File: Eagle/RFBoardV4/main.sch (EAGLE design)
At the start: 32 parts, among them Q1 8/16/20MHz, U1 ATMEGA328

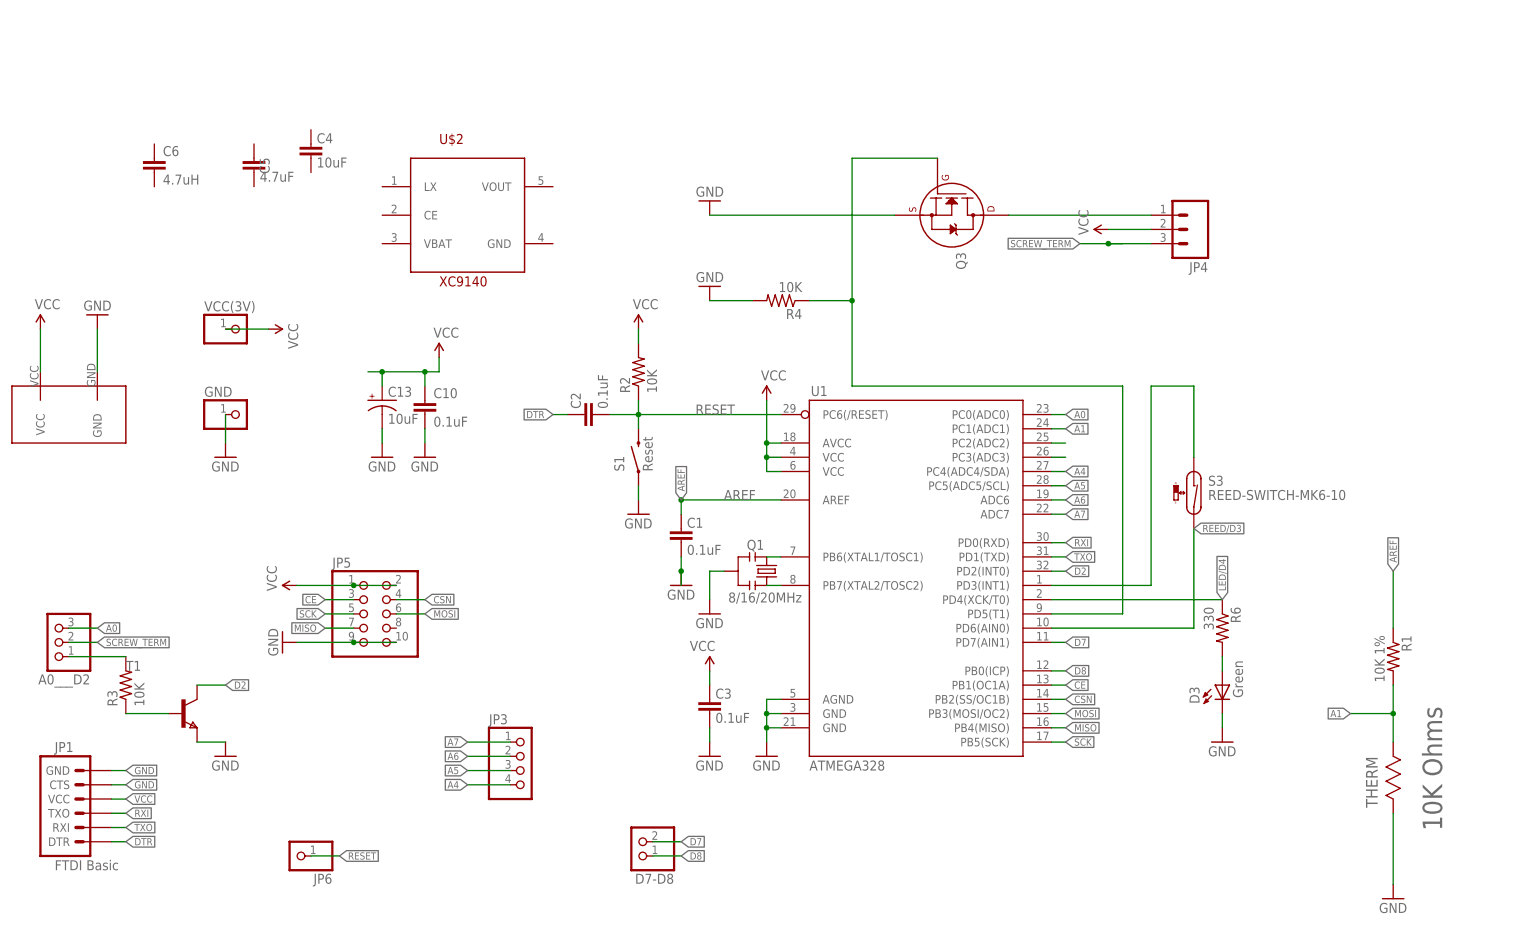
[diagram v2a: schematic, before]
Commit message: Added 3.3v boost circuit to output
- removed transistor that turns aux power on/off
- used boost IC instead
- The aux power now has 3.3v and is useful for PIR solutions
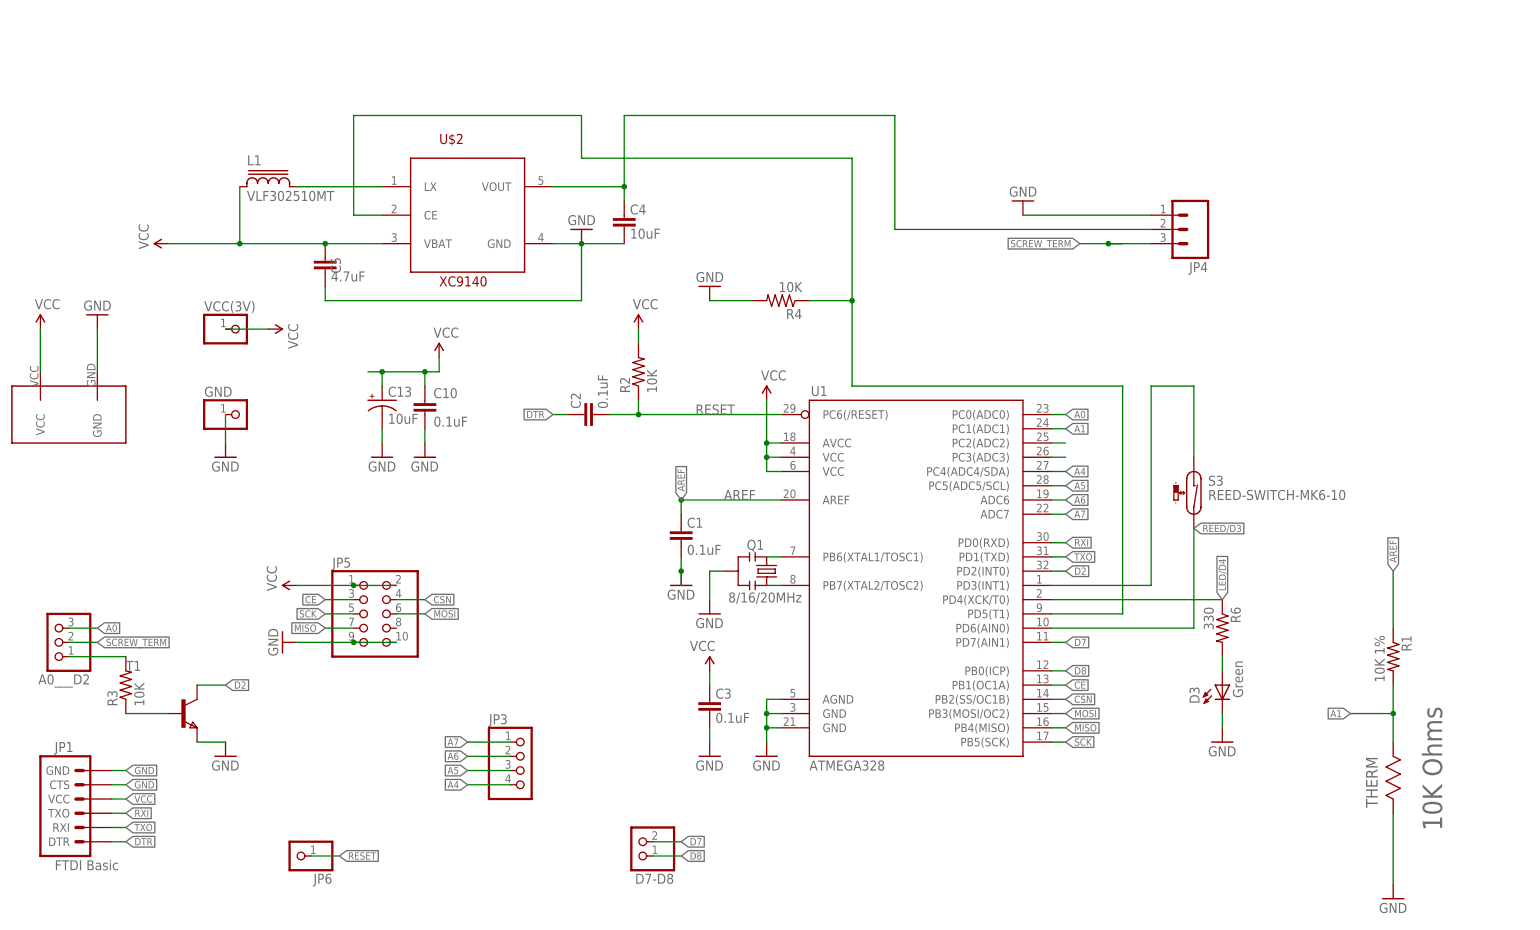
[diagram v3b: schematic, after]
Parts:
- removed C6: 4.7uH, SparkFun:CAP0805
- removed Q3: (no value), transistors:2N7002_SOT23
- removed S1: Reset, Testing:SWITCH-MOMENTARY-2SMD-ALT01
- added L1: VLF302510MT, inductor-tdk:VLF302510MT
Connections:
- removed net N$4: JP4.1, Q3.D
- new net N$8: L1.2, U$2.LX
- new net REG_3.3V: C4.2, JP4.2, U$2.VOUT
- net D5: now also U$2.CE; no longer Q3.G
- net GND: now also C4.1, C5.1, U$2.GND; no longer Q3.S, S1.1
- net RESET: no longer S1.2
- net VCC: now also C5.2, L1.1, U$2.VBAT; no longer JP4.2
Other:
- moved on the sheet: C4, C5
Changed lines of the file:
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@@
 <part name="GND26" library="SparkFun" deviceset="GND" device=""/>
 <part name="R2" library="SparkFun" deviceset="RESISTOR" device="0603-RES" value="10K"/>
-<part name="GND3" library="SparkFun" deviceset="GND" device=""/>
 <part name="C3" library="SparkFun" deviceset="CAP" device="0603-CAP" value="0.1uF"/>
 <part name="GND1" library="SparkFun" deviceset="GND" device=""/>
@@
 <part name="C2" library="SparkFun" deviceset="CAP" device="0603-CAP" value="0.1uF"/>
 <part name="P+4" library="SparkFun" deviceset="3.3V" device="" value="VCC"/>
-<part name="S1" library="Testing" deviceset="SWITCH-MOMENTARY-2" device="SMD-ALT01" value="Reset"/>
 <part name="Q1" library="Testing" deviceset="RESONATOR" device="1:1" value="8/16/20MHz"/>
 <part name="VCC(3V)" library="pinhead" deviceset="PINHD-1X1" device=""/>
@@
 <part name="R3" library="SparkFun" deviceset="RESISTOR" device="0603-RES" value="10K"/>
 <part name="JP4" library="SparkFun-Connectors" deviceset="M03" device="SCREW"/>
-<part name="P+5" library="SparkFun" deviceset="3.3V" device="" value="VCC"/>
 <part name="GND10" library="SparkFun" deviceset="GND" device=""/>
 <part name="R4" library="SparkFun" deviceset="RESISTOR" device="0603-RES" value="10K"/>
 <part name="GND11" library="SparkFun" deviceset="GND" device=""/>
-<part name="Q3" library="transistors" deviceset="2N700*" device="_SOT23" technology="2"/>
 <part name="U$1" library="battery_wilkie" deviceset="BAT" device=""/>
 <part name="P+6" library="SparkFun" deviceset="3.3V" device="" value="VCC"/>
@@
 <part name="C4" library="SparkFun" deviceset="CAP" device="0603-CAP" value="10uF"/>
 <part name="C5" library="SparkFun" deviceset="CAP" device="0603-CAP" value="4.7uF"/>
-<part name="C6" library="SparkFun" deviceset="CAP" device="0805" value="4.7uH"/>
+<part name="L1" library="inductor-tdk" deviceset="VLF302510MT" device=""/>
+<part name="P+7" library="SparkFun" deviceset="3.3V" device="" value="VCC"/>
+<part name="GND14" library="SparkFun" deviceset="GND" device=""/>
 </parts>
 <sheets>
@@
 <instance part="GND26" gate="1" x="83.82" y="147.32"/>
 <instance part="R2" gate="G$1" x="121.92" y="162.56" rot="R90"/>
-<instance part="GND3" gate="1" x="121.92" y="137.16"/>
 <instance part="C3" gate="G$1" x="134.62" y="104.14" smashed="yes" rot="R180">
 <attribute name="NAME" x="135.636" y="104.267" size="1.778" layer="95"/>
@@
 </instance>
 <instance part="P+4" gate="G$1" x="86.36" y="165.1"/>
-<instance part="S1" gate="G$1" x="121.92" y="147.32" rot="R90"/>
 <instance part="Q1" gate="G$1" x="144.78" y="127" smashed="yes" rot="R270">
 <attribute name="NAME" x="141.224" y="130.81" size="1.778" layer="95"/>
@@
 <instance part="R3" gate="G$1" x="30.48" y="106.68" rot="R90"/>
 <instance part="JP4" gate="G$1" x="220.98" y="187.96" rot="R180"/>
-<instance part="P+5" gate="G$1" x="205.74" y="187.96" rot="R90"/>
-<instance part="GND10" gate="1" x="134.62" y="193.04" rot="R180"/>
+<instance part="GND10" gate="1" x="190.5" y="193.04" rot="R180"/>
 <instance part="R4" gate="G$1" x="147.32" y="175.26" rot="R180"/>
 <instance part="GND11" gate="1" x="134.62" y="177.8" rot="R180"/>
-<instance part="Q3" gate="G$1" x="177.8" y="190.5" rot="R270"/>
 <instance part="U$1" gate="G$1" x="43.18" y="147.32"/>
 <instance part="P+6" gate="G$1" x="15.24" y="170.18"/>
 <instance part="GND12" gate="1" x="25.4" y="172.72" rot="R180"/>
 <instance part="U$2" gate="IC1" x="91.44" y="190.5"/>
-<instance part="C4" gate="G$1" x="63.5" y="203.2" smashed="yes" rot="R180">
-<attribute name="NAME" x="64.516" y="203.327" size="1.778" layer="95"/>
-<attribute name="VALUE" x="64.516" y="199.009" size="1.778" layer="96"/>
-</instance>
-<instance part="C5" gate="G$1" x="53.34" y="200.66" smashed="yes" rot="R180">
-<attribute name="NAME" x="54.356" y="200.787" size="1.778" layer="95" rot="R270"/>
-<attribute name="VALUE" x="54.356" y="196.469" size="1.778" layer="96"/>
-</instance>
-<instance part="C6" gate="G$1" x="35.56" y="198.12"/>
+<instance part="C4" gate="G$1" x="119.38" y="190.5" smashed="yes" rot="R180">
+<attribute name="NAME" x="120.396" y="190.627" size="1.778" layer="95"/>
+<attribute name="VALUE" x="120.396" y="186.309" size="1.778" layer="96"/>
+</instance>
+<instance part="C5" gate="G$1" x="66.04" y="182.88" smashed="yes" rot="R180">
+<attribute name="NAME" x="67.056" y="183.007" size="1.778" layer="95" rot="R270"/>
+<attribute name="VALUE" x="67.056" y="178.689" size="1.778" layer="96"/>
+</instance>
+<instance part="L1" gate="G$1" x="55.88" y="195.58"/>
+<instance part="P+7" gate="G$1" x="38.1" y="185.42" rot="R90"/>
+<instance part="GND14" gate="1" x="111.76" y="187.96" rot="R180"/>
 </instances>
 <busses>
@@
 <pinref part="C10" gate="G$1" pin="2"/>
 <pinref part="GND26" gate="1" pin="GND"/>
-</segment>
-<segment>
-<wire x1="121.92" y1="142.24" x2="121.92" y2="139.7" width="0.1524" layer="91"/>
-<pinref part="GND3" gate="1" pin="GND"/>
-<pinref part="S1" gate="G$1" pin="1"/>
 </segment>
 <segment>
@@
 </segment>
 <segment>
-<pinref part="Q3" gate="G$1" pin="S"/>
 <pinref part="GND10" gate="1" pin="GND"/>
-<wire x1="167.64" y1="190.5" x2="134.62" y2="190.5" width="0.1524" layer="91"/>
+<wire x1="213.36" y1="190.5" x2="190.5" y2="190.5" width="0.1524" layer="91"/>
+</segment>
+<segment>
+<pinref part="U$2" gate="IC1" pin="GND"/>
+<pinref part="GND14" gate="1" pin="GND"/>
+<wire x1="106.68" y1="185.42" x2="111.76" y2="185.42" width="0.1524" layer="91"/>
+<wire x1="111.76" y1="185.42" x2="111.76" y2="175.26" width="0.1524" layer="91"/>
+<junction x="111.76" y="185.42"/>
+<wire x1="111.76" y1="175.26" x2="66.04" y2="175.26" width="0.1524" layer="91"/>
+<pinref part="C5" gate="G$1" pin="1"/>
+<wire x1="66.04" y1="175.26" x2="66.04" y2="177.8" width="0.1524" layer="91"/>
+<pinref part="C4" gate="G$1" pin="1"/>
+<wire x1="119.38" y1="185.42" x2="111.76" y2="185.42" width="0.1524" layer="91"/>
 </segment>
 </net>
@@
 <wire x1="147.32" y1="154.94" x2="121.92" y2="154.94" width="0.1524" layer="91"/>
 <wire x1="121.92" y1="157.48" x2="121.92" y2="154.94" width="0.1524" layer="91"/>
-<wire x1="121.92" y1="152.4" x2="121.92" y2="154.94" width="0.1524" layer="91"/>
 <wire x1="121.92" y1="154.94" x2="116.84" y2="154.94" width="0.1524" layer="91"/>
 <junction x="121.92" y="154.94"/>
@@
 <pinref part="R2" gate="G$1" pin="1"/>
 <pinref part="C2" gate="G$1" pin="1"/>
-<pinref part="S1" gate="G$1" pin="2"/>
 </segment>
 </net>
@@
 </segment>
 <segment>
-<pinref part="JP4" gate="G$1" pin="2"/>
-<pinref part="P+5" gate="G$1" pin="3.3V"/>
-<wire x1="213.36" y1="187.96" x2="205.74" y2="187.96" width="0.1524" layer="91"/>
-</segment>
-<segment>
 <pinref part="P+6" gate="G$1" pin="3.3V"/>
 <pinref part="U$1" gate="G$1" pin="VCC"/>
 <wire x1="15.24" y1="170.18" x2="15.24" y2="162.56" width="0.1524" layer="91"/>
+</segment>
+<segment>
+<pinref part="U$2" gate="IC1" pin="VBAT"/>
+<pinref part="P+7" gate="G$1" pin="3.3V"/>
+<wire x1="76.2" y1="185.42" x2="66.04" y2="185.42" width="0.1524" layer="91"/>
+<pinref part="L1" gate="G$1" pin="1"/>
+<wire x1="66.04" y1="185.42" x2="50.8" y2="185.42" width="0.1524" layer="91"/>
+<wire x1="50.8" y1="185.42" x2="38.1" y2="185.42" width="0.1524" layer="91"/>
+<wire x1="50.8" y1="195.58" x2="50.8" y2="185.42" width="0.1524" layer="91"/>
+<junction x="50.8" y="185.42"/>
+<pinref part="C5" gate="G$1" pin="2"/>
+<junction x="66.04" y="185.42"/>
 </segment>
 </net>
@@
 <pinref part="R4" gate="G$1" pin="1"/>
 <wire x1="152.4" y1="175.26" x2="160.02" y2="175.26" width="0.1524" layer="91"/>
-<pinref part="Q3" gate="G$1" pin="G"/>
 <junction x="160.02" y="175.26"/>
 <wire x1="160.02" y1="175.26" x2="160.02" y2="200.66" width="0.1524" layer="91"/>
-<wire x1="160.02" y1="200.66" x2="175.26" y2="200.66" width="0.1524" layer="91"/>
+<pinref part="U$2" gate="IC1" pin="CE"/>
+<wire x1="76.2" y1="190.5" x2="71.12" y2="190.5" width="0.1524" layer="91"/>
+<wire x1="71.12" y1="190.5" x2="71.12" y2="208.28" width="0.1524" layer="91"/>
+<wire x1="71.12" y1="208.28" x2="111.76" y2="208.28" width="0.1524" layer="91"/>
+<wire x1="111.76" y1="208.28" x2="111.76" y2="200.66" width="0.1524" layer="91"/>
+<wire x1="111.76" y1="200.66" x2="160.02" y2="200.66" width="0.1524" layer="91"/>
 </segment>
 </net>
@@
 </segment>
 </net>
-<net name="N$4" class="2">
-<segment>
-<pinref part="JP4" gate="G$1" pin="1"/>
-<pinref part="Q3" gate="G$1" pin="D"/>
-<wire x1="213.36" y1="190.5" x2="187.96" y2="190.5" width="0.1524" layer="91"/>
-</segment>
-</net>
+<net name="REG_3.3V" class="0">
+<segment>
+<pinref part="U$2" gate="IC1" pin="VOUT"/>
+<wire x1="106.68" y1="195.58" x2="119.38" y2="195.58" width="0.1524" layer="91"/>
+<wire x1="119.38" y1="195.58" x2="119.38" y2="208.28" width="0.1524" layer="91"/>
+<wire x1="119.38" y1="208.28" x2="167.64" y2="208.28" width="0.1524" layer="91"/>
+<wire x1="167.64" y1="208.28" x2="167.64" y2="187.96" width="0.1524" layer="91"/>
+<pinref part="JP4" gate="G$1" pin="2"/>
+<wire x1="167.64" y1="187.96" x2="213.36" y2="187.96" width="0.1524" layer="91"/>
+<pinref part="C4" gate="G$1" pin="2"/>
+<wire x1="119.38" y1="193.04" x2="119.38" y2="195.58" width="0.1524" layer="91"/>
+<junction x="119.38" y="195.58"/>
+</segment>
+</net>
+<net name="N$8" class="0">
+<segment>
+<pinref part="U$2" gate="IC1" pin="LX"/>
+<pinref part="L1" gate="G$1" pin="2"/>
+<wire x1="76.2" y1="195.58" x2="60.96" y2="195.58" width="0.1524" layer="91"/>
+</segment>
+</net>

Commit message: V4.3 - Better option for int and reed
Added two pins for more reed options.  this also gives the ability to
choose the reverse or not for the interrupts
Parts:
- added D7-D1: (no value), pinhead:PINHD-1X2
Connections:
- net N$3 renamed D2_VIA_FET
- net REED/D3 renamed REED/D6
- removed net REED_INT: S3.1, U1.PD3(INT1)
- new net D2_INT0: U1.PD2(INT0)
- new net D3_INT1: D7-D1.2, U1.PD3(INT1)
- new net REED: D7-D1.1, S3.1
- net D2: no longer U1.PD2(INT0)
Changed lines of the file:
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@@
 <part name="P+7" library="SparkFun" deviceset="3.3V" device="" value="VCC"/>
 <part name="GND14" library="SparkFun" deviceset="GND" device=""/>
+<part name="D7-D1" library="pinhead" deviceset="PINHD-1X2" device=""/>
 </parts>
 <sheets>
@@
 <instance part="P+7" gate="G$1" x="38.1" y="185.42" rot="R90"/>
 <instance part="GND14" gate="1" x="111.76" y="187.96" rot="R180"/>
+<instance part="D7-D1" gate="G$1" x="17.78" y="124.46" rot="R180"/>
 </instances>
 <busses>
@@
 </segment>
 </net>
-<net name="REED/D3" class="0">
+<net name="REED/D6" class="0">
 <segment>
 <label x="220.98" y="134.62" size="1.27" layer="95" xref="yes"/>
@@
 </net>
 <net name="D2" class="0">
-<segment>
-<pinref part="U1" gate="G$1" pin="PD2(INT0)"/>
-<wire x1="195.58" y1="127" x2="198.12" y2="127" width="0.1524" layer="91"/>
-<label x="198.12" y="127" size="1.27" layer="95" xref="yes"/>
-</segment>
 <segment>
 <pinref part="T1" gate="A" pin="C"/>
@@
 </segment>
 </net>
-<net name="N$3" class="0">
+<net name="D2_VIA_FET" class="0">
 <segment>
 <pinref part="A0___D2" gate="A" pin="1"/>
@@
 </segment>
 </net>
-<net name="REED_INT" class="0">
-<segment>
-<pinref part="S3" gate="G$1" pin="1"/>
-<wire x1="213.36" y1="160.02" x2="220.98" y2="160.02" width="0.1524" layer="91"/>
-<wire x1="220.98" y1="160.02" x2="220.98" y2="147.32" width="0.1524" layer="91"/>
+<net name="D3_INT1" class="0">
+<segment>
 <pinref part="U1" gate="G$1" pin="PD3(INT1)"/>
-<wire x1="195.58" y1="124.46" x2="213.36" y2="124.46" width="0.1524" layer="91"/>
-<wire x1="213.36" y1="124.46" x2="213.36" y2="160.02" width="0.1524" layer="91"/>
+<wire x1="195.58" y1="124.46" x2="198.12" y2="124.46" width="0.1524" layer="91"/>
+<label x="198.12" y="124.46" size="1.27" layer="95" xref="yes"/>
+</segment>
+<segment>
+<pinref part="D7-D1" gate="G$1" pin="2"/>
+<wire x1="20.32" y1="124.46" x2="25.4" y2="124.46" width="0.1524" layer="91"/>
+<label x="25.4" y="124.46" size="1.27" layer="95" xref="yes"/>
 </segment>
 </net>
@@
 </segment>
 </net>
+<net name="D2_INT0" class="0">
+<segment>
+<pinref part="U1" gate="G$1" pin="PD2(INT0)"/>
+<wire x1="195.58" y1="127" x2="198.12" y2="127" width="0.1524" layer="91"/>
+<label x="198.12" y="127" size="1.27" layer="95" xref="yes"/>
+</segment>
+</net>
+<net name="REED" class="0">
+<segment>
+<pinref part="S3" gate="G$1" pin="1"/>
+<wire x1="220.98" y1="147.32" x2="220.98" y2="152.4" width="0.1524" layer="91"/>
+<label x="220.98" y="152.4" size="1.27" layer="95" xref="yes"/>
+</segment>
+<segment>
+<pinref part="D7-D1" gate="G$1" pin="1"/>
+<wire x1="20.32" y1="121.92" x2="25.4" y2="121.92" width="0.1524" layer="91"/>
+<label x="25.4" y="121.92" size="1.27" layer="95" xref="yes"/>
+</segment>
+</net>

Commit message: Fixed boost, board improvements
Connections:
- net GND: now also JP4.1
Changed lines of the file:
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@@
-</segment>
-<segment>
-<pinref part="GND10" gate="1" pin="GND"/>
-<wire x1="213.36" y1="190.5" x2="190.5" y2="190.5" width="0.1524" layer="91"/>
 </segment>
 <segment>
@@
 <wire x1="119.38" y1="185.42" x2="111.76" y2="185.42" width="0.1524" layer="91"/>
 </segment>
+<segment>
+<pinref part="JP4" gate="G$1" pin="1"/>
+<pinref part="GND10" gate="1" pin="GND"/>
+<wire x1="213.36" y1="190.5" x2="190.5" y2="190.5" width="0.1524" layer="91"/>
+</segment>
 </net>

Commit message: 4.3 checked in
- Reed can now be connected to either interrupt
- Fixed pads for the 3.3 boost circuit
- General improvements
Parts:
- L1: value VLF302510MT -> VLF302512MT; device inductor-tdk:VLF302510MT -> inductor-tdk:VLF302512MT
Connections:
- removed net D2: T1.C
- net D2_INT0: now also T1.C
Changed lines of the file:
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@@
 <part name="C4" library="SparkFun" deviceset="CAP" device="0603-CAP" value="10uF"/>
 <part name="C5" library="SparkFun" deviceset="CAP" device="0603-CAP" value="4.7uF"/>
-<part name="L1" library="inductor-tdk" deviceset="VLF302510MT" device=""/>
+<part name="L1" library="inductor-tdk" deviceset="VLF302512MT" device=""/>
 <part name="P+7" library="SparkFun" deviceset="3.3V" device="" value="VCC"/>
 <part name="GND14" library="SparkFun" deviceset="GND" device=""/>
@@
 </segment>
 </net>
-<net name="D2" class="0">
-<segment>
-<pinref part="T1" gate="A" pin="C"/>
-<wire x1="43.18" y1="106.68" x2="48.26" y2="106.68" width="0.1524" layer="91"/>
-<label x="48.26" y="106.68" size="1.27" layer="95" xref="yes"/>
-</segment>
-</net>
 <net name="A0" class="0">
 <segment>
@@
 <label x="198.12" y="127" size="1.27" layer="95" xref="yes"/>
 </segment>
-</net>
+<segment>
+<pinref part="T1" gate="A" pin="C"/>
+<wire x1="43.18" y1="106.68" x2="48.26" y2="106.68" width="0.1524" layer="91"/>
+<label x="48.26" y="106.68" size="1.27" layer="95" xref="yes"/>
+</segment>
+</net>
